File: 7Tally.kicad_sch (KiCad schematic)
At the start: 20 parts, among them SW1 TL3300CF160Q, U1 ESP32-C3_SUPERMINI_TH, U2 BQ21040DBVR, U3 TC1263-3.3VOA

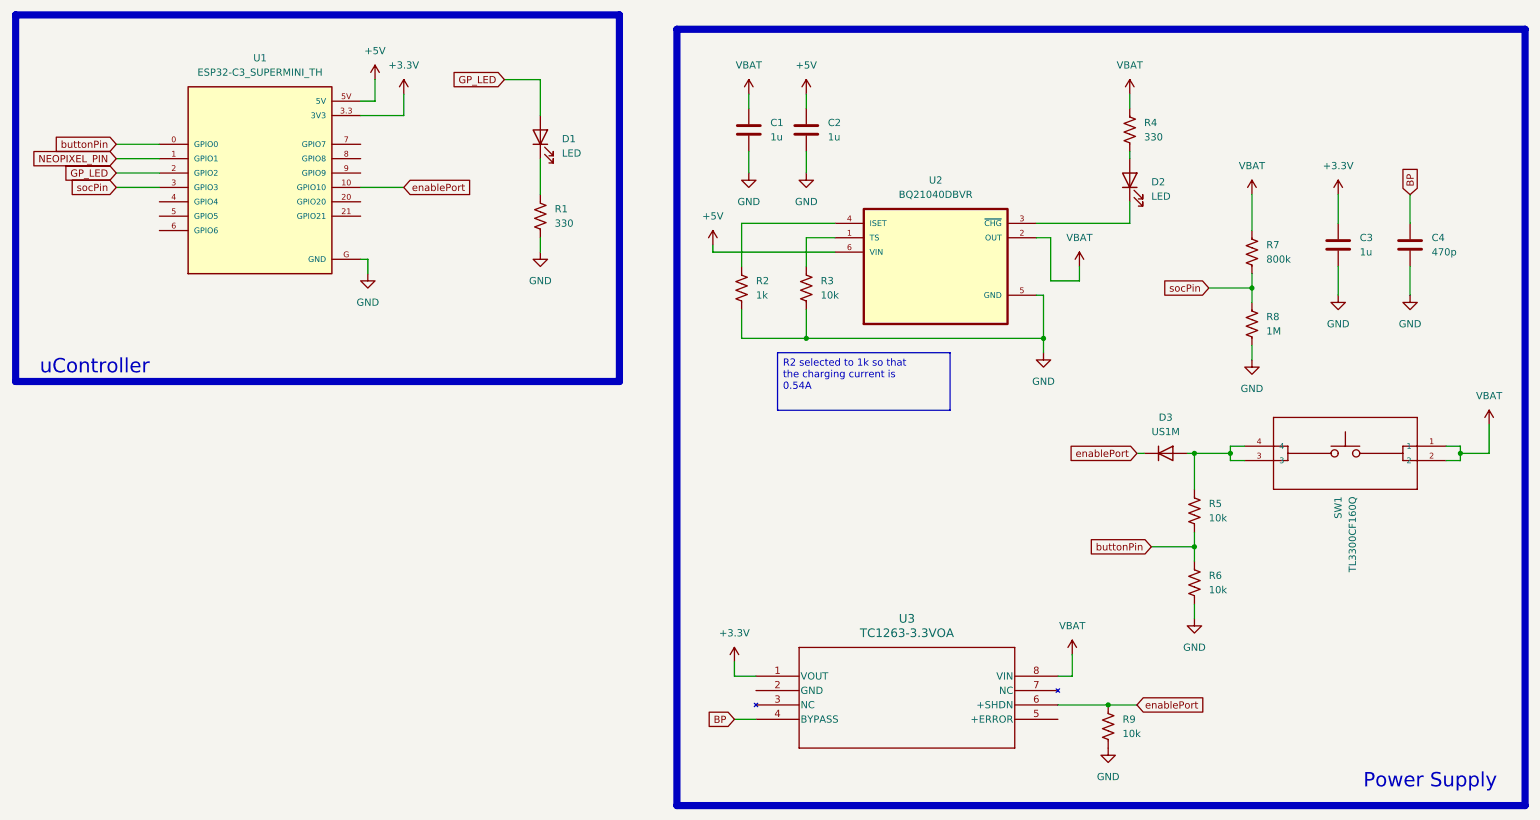
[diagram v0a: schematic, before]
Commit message: schematic: added connectors
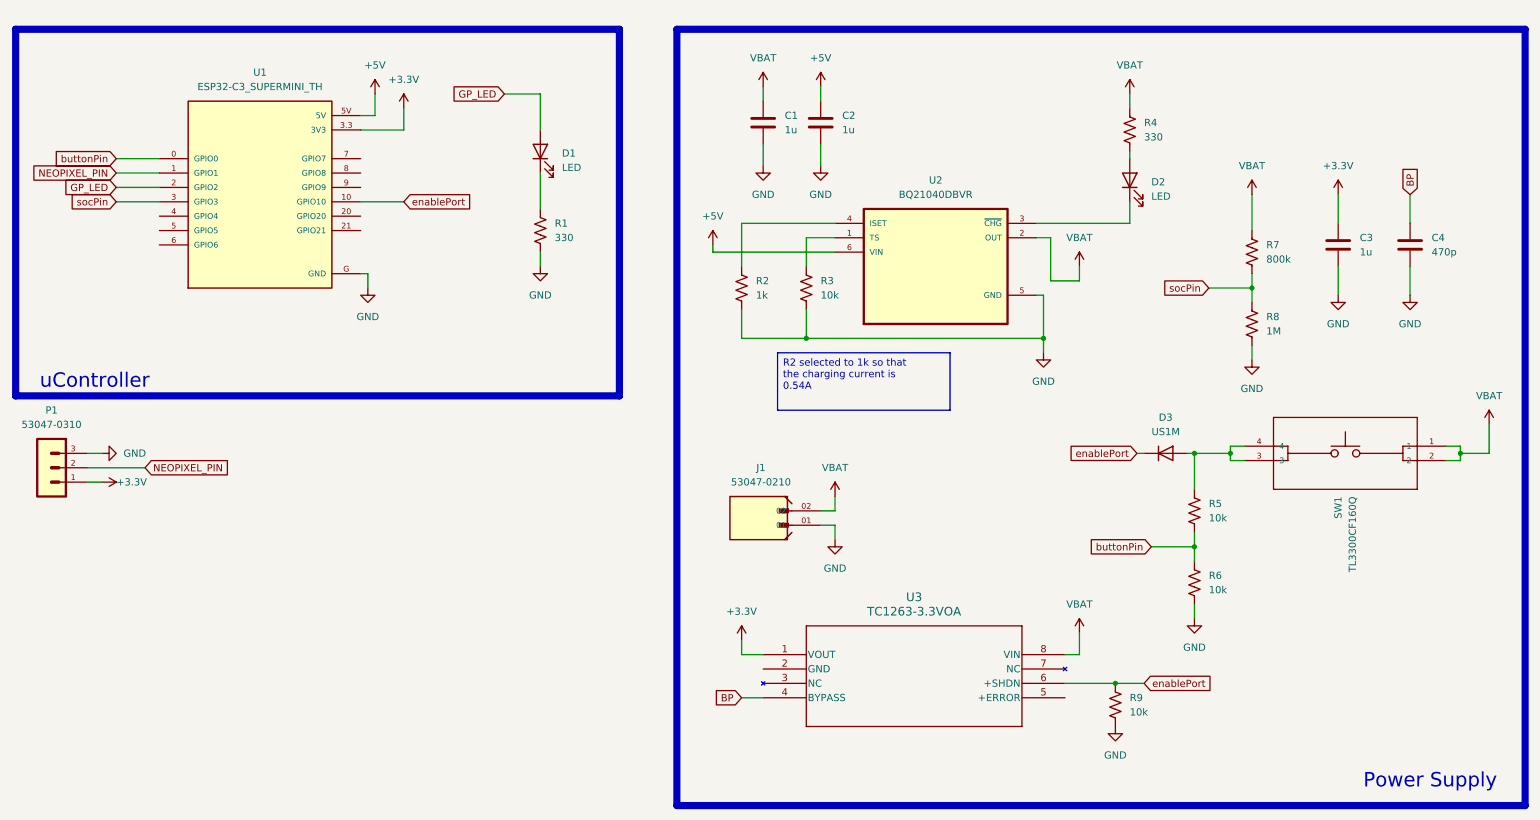
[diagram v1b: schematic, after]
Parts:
- added J1: 53047-0210, 53047-0210:MOLEX_53047-0210, symbol 53047-0210:53047-0210
- added P1: 53047-0310, 53047-0310:53047-0310, symbol 53047-0310:53047-0310
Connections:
- net +3.3V: now also P1.1
- net GND: now also J1.01, P1.3
- net NEOPIXEL_PIN: now also P1.2
- net VBAT: now also J1.02
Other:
- company: (none) -> Hazcompany
- title: (none) -> 7Tally
- moved on the sheet: C1, C2, D1, R1, R9, U1, U3

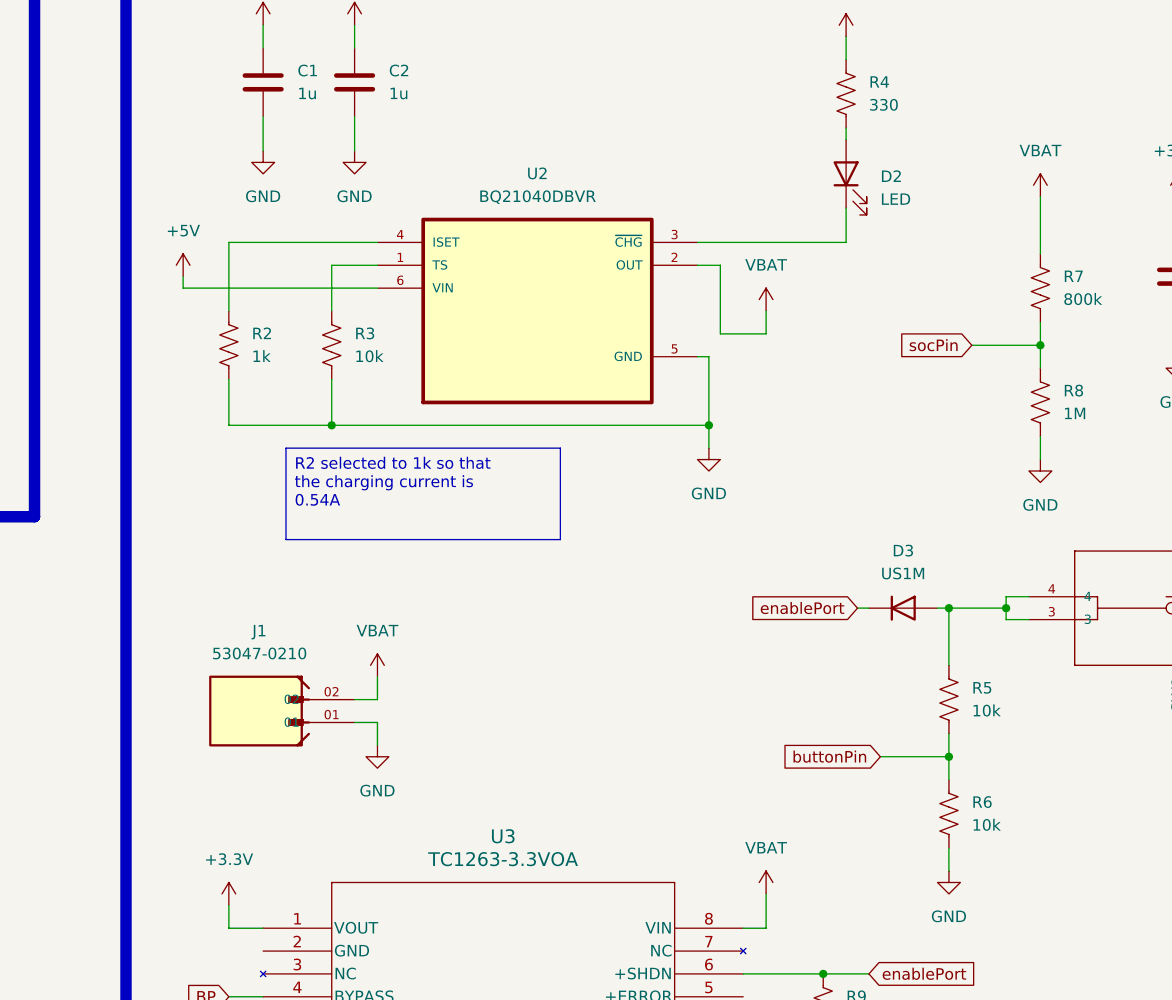
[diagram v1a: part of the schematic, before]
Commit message: schematic:error fix
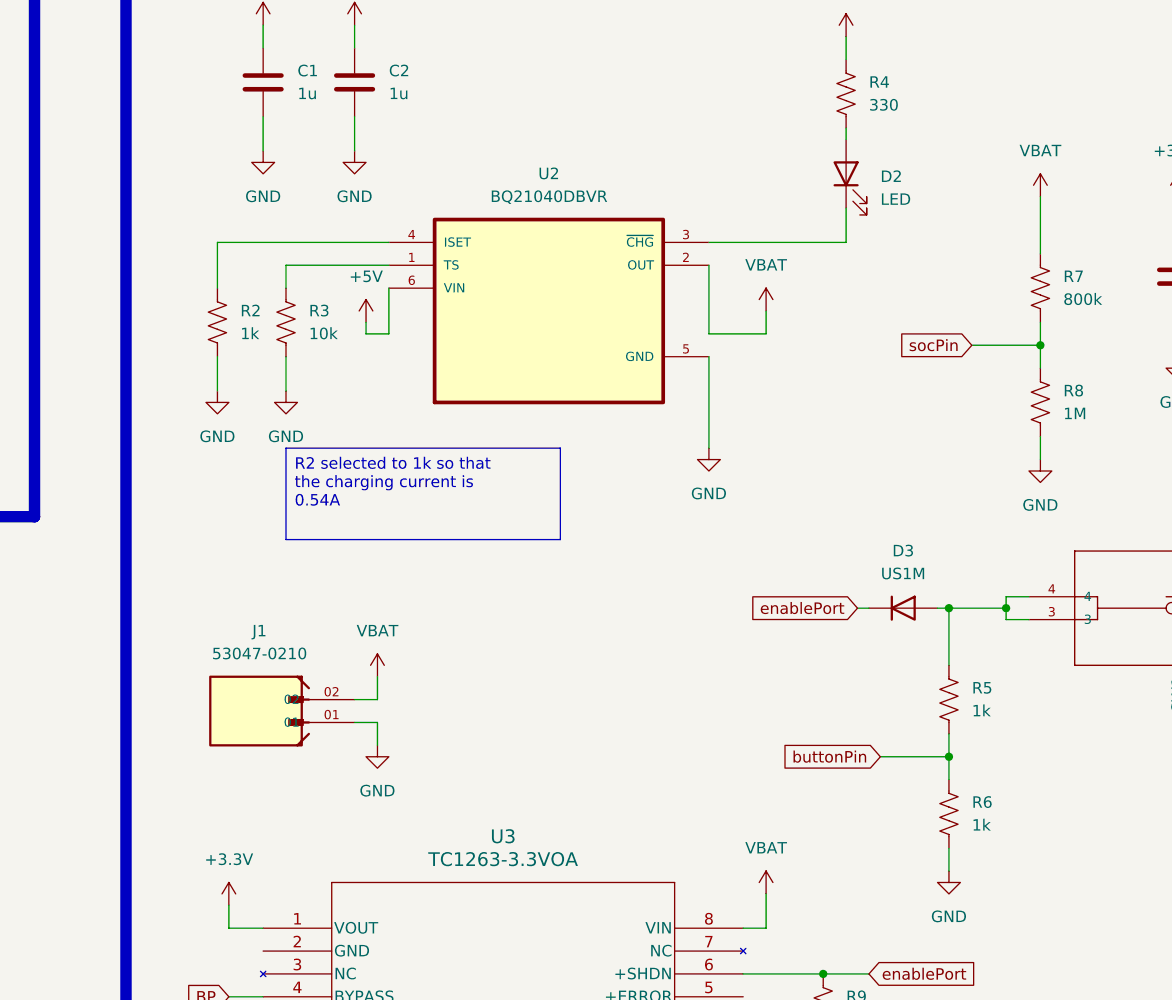
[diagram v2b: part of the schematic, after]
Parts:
- R5, R6: value 10k -> 1k
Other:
- moved on the sheet: R2, R3, U2

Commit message: feat(DRC): Imported DRC rules from JLCPCB
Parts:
- U3: footprint SOIC8-N_MC_MCH -> TC1263-3-3VOA:TC1263-3-3VOA_SOIC8-N_MC_MCH
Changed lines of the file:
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@@
 			)
 		)
-		(property "Footprint" "SOIC8-N_MC_MCH"
+		(property "Footprint" "TC1263-3-3VOA:TC1263-3-3VOA_SOIC8-N_MC_MCH"
 			(at 147.32 127 0)
 			(effects

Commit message: chore(PCB): added 3D models and start PCB
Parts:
- removed D3: US1M, Diode_SMD:D_SMA, symbol Diode:US1M
- removed J1: 53047-0210, 53047-0210:MOLEX_53047-0210, symbol 53047-0210:53047-0210
- added D4: ESD7351XV2T1G, ESD7351XV2T1G:SOD-523-2_ONSEMI, symbol ESD7351XV2T1G:ESD7351XV2T1G
- added J2: B2B-PH-K-S_LF__SN_, B2B-PH-K-S_LF__SN_:JST_B2B-PH-K-S_LF__SN_, symbol B2B-PH-K-S_LF__SN_:B2B-PH-K-S_LF__SN_
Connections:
- net GND: now also J2.1
- net VBAT: now also J2.2
- net enablePort: now also D4.1
- net at R5.1, SW1.3, SW1.4: now also D4.2

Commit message: feat(PCB): start of routing
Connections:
- net GND: now also U3.2 (GND)
- no-connect marks 0 -> 9
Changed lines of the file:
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@@
 		(color 0 0 0 0)
 	)
+	(no_connect
+		(at 76.2 44.45)
+	)
+	(no_connect
+		(at 40.64 49.53)
+	)
+	(no_connect
+		(at 40.64 54.61)
+	)
+	(no_connect
+		(at 76.2 49.53)
+	)
+	(no_connect
+		(at 76.2 41.91)
+	)
+	(no_connect
+		(at 40.64 52.07)
+	)
+	(no_connect
+		(at 76.2 39.37)
+	)
+	(no_connect
+		(at 200.66 134.62)
+	)
+	(no_connect
+		(at 76.2 52.07)
+	)
 	(wire
 		(pts
@@
 	(wire
 		(pts
+			(xy 144.78 130.81) (xy 144.78 129.54)
+		)
+		(stroke
+			(width 0)
+			(type default)
+		)
+	)
+	(wire
+		(pts
 			(xy 203.2 127) (xy 203.2 123.19)
 		)
@@
 		(pts
 			(xy 142.24 63.5) (xy 142.24 67.31)
+		)
+		(stroke
+			(width 0)
+			(type default)
+		)
+	)
+	(wire
+		(pts
+			(xy 144.78 129.54) (xy 147.32 129.54)
 		)
 		(stroke
@@
 	)
 	(symbol
-		(lib_id "power:+5V")
-		(at 78.74 27.94 0)
-		(unit 1)
-		(exclude_from_sim no)
-		(in_bom yes)
-		(on_board yes)
-		(dnp no)
-		(fields_autoplaced yes)
-		(property "Reference" "#PWR01"
-			(at 78.74 31.75 0)
-			(effects
-				(font
-					(size 1.27 1.27)
-				)
-				(hide yes)
-			)
-		)
-		(property "Value" "+5V"
-			(at 78.74 22.86 0)
-			(effects
-				(font
-					(size 1.27 1.27)
-				)
-			)
-		)
-		(property "Footprint" ""
-			(at 78.74 27.94 0)
-			(effects
-				(font
-					(size 1.27 1.27)
-				)
-				(hide yes)
-			)
-		)
-		(property "Datasheet" ""
-			(at 78.74 27.94 0)
-			(effects
-				(font
-					(size 1.27 1.27)
-				)
-				(hide yes)
-			)
-		)
-		(property "Description" "Power symbol creates a global label with name \"+5V\""
-			(at 78.74 27.94 0)
-			(effects
-				(font
-					(size 1.27 1.27)
-				)
-				(hide yes)
-			)
-		)
-		(pin "1"
-		)
-		(instances
-			(project ""
-				(path "/a26cb5f3-8ba9-4d03-a29e-a58d33583019"
-					(reference "#PWR01")
-					(unit 1)
-				)
-			)
-		)
-	)
-	(symbol
 		(lib_id "Device:LED")
 		(at 212.09 43.18 90)
@@
 	)
 	(symbol
+		(lib_id "power:+5V")
+		(at 78.74 27.94 0)
+		(unit 1)
+		(exclude_from_sim no)
+		(in_bom yes)
+		(on_board yes)
+		(dnp no)
+		(fields_autoplaced yes)
+		(property "Reference" "#PWR07"
+			(at 78.74 31.75 0)
+			(effects
+				(font
+					(size 1.27 1.27)
+				)
+				(hide yes)
+			)
+		)
+		(property "Value" "+5V"
+			(at 78.74 22.86 0)
+			(effects
+				(font
+					(size 1.27 1.27)
+				)
+			)
+		)
+		(property "Footprint" ""
+			(at 78.74 27.94 0)
+			(effects
+				(font
+					(size 1.27 1.27)
+				)
+				(hide yes)
+			)
+		)
+		(property "Datasheet" ""
+			(at 78.74 27.94 0)
+			(effects
+				(font
+					(size 1.27 1.27)
+				)
+				(hide yes)
+			)
+		)
+		(property "Description" "Power symbol creates a global label with name \"+5V\""
+			(at 78.74 27.94 0)
+			(effects
+				(font
+					(size 1.27 1.27)
+				)
+				(hide yes)
+			)
+		)
+		(pin "1"
+		)
+		(instances
+			(project "7Tally"
+				(path "/a26cb5f3-8ba9-4d03-a29e-a58d33583019"
+					(reference "#PWR07")
+					(unit 1)
+				)
+			)
+		)
+	)
+	(symbol
 		(lib_id "BQ21040DBVR:BQ21040DBVR")
 		(at 179.07 58.42 0)
@@
 					(unit 1)
 				)
+			)
+		)
+	)
+	(symbol
+		(lib_id "power:GND")
+		(at 144.78 130.81 0)
+		(unit 1)
+		(exclude_from_sim no)
+		(in_bom yes)
+		(on_board yes)
+		(dnp no)
+		(property "Reference" "#PWR029"
+			(at 144.78 137.16 0)
+			(effects
+				(font
+					(size 1.27 1.27)
+				)
+				(hide yes)
+			)
+		)
+		(property "Value" "GND"
+			(at 141.986 131.064 0)
+			(effects
+				(font
+					(size 1.27 1.27)
+				)
+			)
+		)
+		(property "Footprint" ""
+			(at 144.78 130.81 0)
+			(effects
+				(font
+					(size 1.27 1.27)
+				)
+				(hide yes)
+			)
+		)
+		(property "Datasheet" ""
+			(at 144.78 130.81 0)
+			(effects
+				(font
+					(size 1.27 1.27)
+				)
+				(hide yes)
+			)
+		)
+		(property "Description" "Power symbol creates a global label with name \"GND\" , ground"
+			(at 144.78 130.81 0)
+			(effects
+				(font
+					(size 1.27 1.27)
+				)
+				(hide yes)
+			)
+		)
+		(pin "1"
+		)
+		(instances
+			(project "7Tally"
+				(path "/a26cb5f3-8ba9-4d03-a29e-a58d33583019"
+					(reference "#PWR029")
+					(unit 1)
+				)

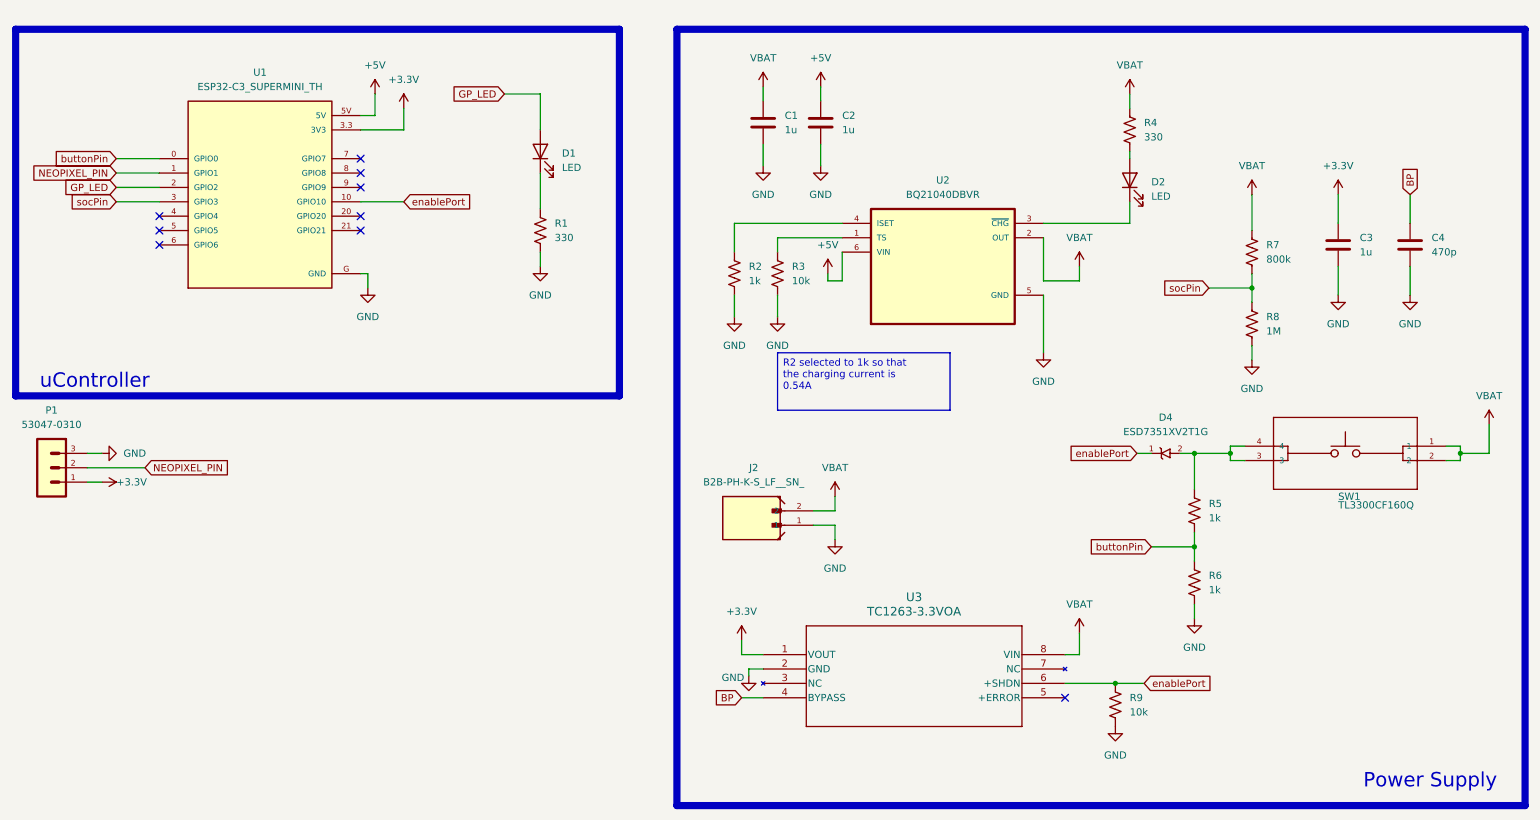
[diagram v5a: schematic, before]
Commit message: feat(PCB): Start leds
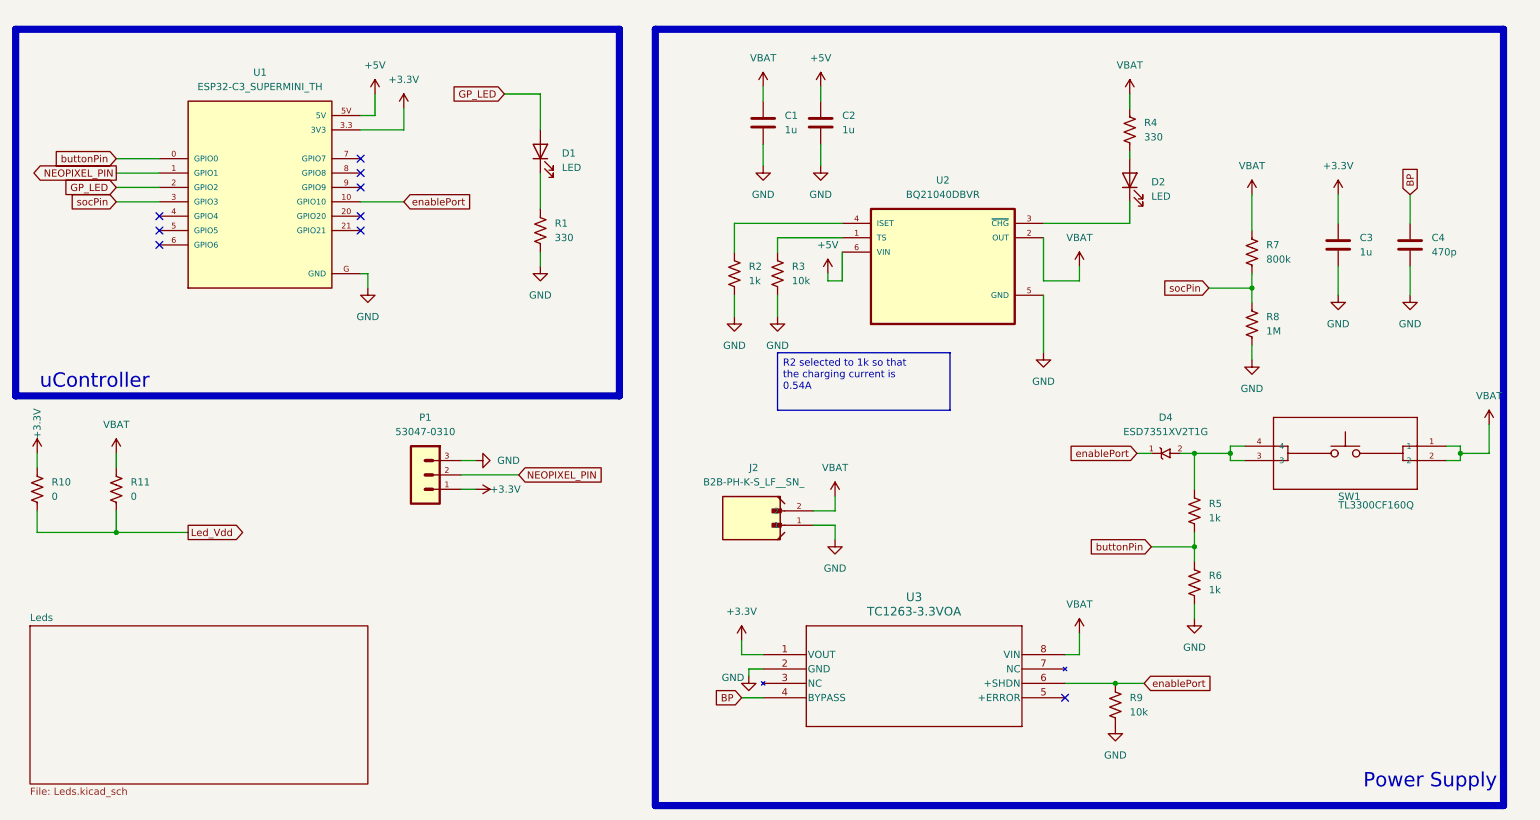
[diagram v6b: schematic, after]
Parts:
- added R10: 0, Resistor_SMD:R_01005_0402Metric, symbol Device:R_US
- added R11: 0, Resistor_SMD:R_0402_1005Metric, symbol Device:R_US
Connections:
- net +3.3V: now also R10.1
- net VBAT: now also R11.1
- new net Led_Vdd: R10.2, R11.2
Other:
- added sheet Leds (Leds.kicad_sch)
- moved on the sheet: P1

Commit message: feat(PCB): start of castellated edges implementation
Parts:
- R10: footprint Resistor_SMD:R_01005_0402Metric -> Resistor_SMD:R_0805_2012Metric
- R11: footprint Resistor_SMD:R_0402_1005Metric -> Resistor_SMD:R_0805_2012Metric
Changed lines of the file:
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@@
 			)
 		)
-		(property "Footprint" "Resistor_SMD:R_01005_0402Metric"
+		(property "Footprint" "Resistor_SMD:R_0805_2012Metric"
 			(at 20.066 98.044 90)
 			(effects
@@
 			)
 		)
-		(property "Footprint" "Resistor_SMD:R_0402_1005Metric"
+		(property "Footprint" "Resistor_SMD:R_0805_2012Metric"
 			(at 34.036 98.044 90)
 			(effects
